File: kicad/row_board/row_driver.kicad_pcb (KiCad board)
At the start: 2 copper layers, 100 x 100 mm, 80 parts, among them J1 Panel row connector (female), J2 Row daisy chain connector (ma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, J3 Conn_01x04, J4 Column Board Connector, J6 Barrel_Jack, J7 Controller A, J8 Controller B, Q1 2N3904, Q2 FQP47P06, U1 TPIC6B595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

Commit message: Mostly routed column board
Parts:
- J2: footprint Connectors:IDC_Header_Straight_40pins -> lib_fp:IDC_Header_Straight_40pins
- J4: footprint Connectors:IDC_Header_Straight_10pins -> lib_fp:IDC_Header_Straight_10pins
- moved J4 2.95 mm to (30.0, 65.0)
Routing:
- net RC_DATA: track 66.6 -> 70.7 mm
- net RC_SHIFT_CLK: track 161.7 -> 165.8 mm
- net GND: track 37.1 -> 34.1 mm, vias 24 -> 23
- net COL_REG_CLK: track 53.5 -> 56.4 mm
- net ~RC_CLEAR: track 146.0 -> 144.5 mm, vias 8 -> 9

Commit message: Add Gerber and DXF files for row and column boards
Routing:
- net +5V: track 393.3 -> 404.1 mm
- net ~ROW_EN: track 112.4 -> 114.4 mm
- net Net-(D104-Pad2): track 50.8 -> 51.9 mm

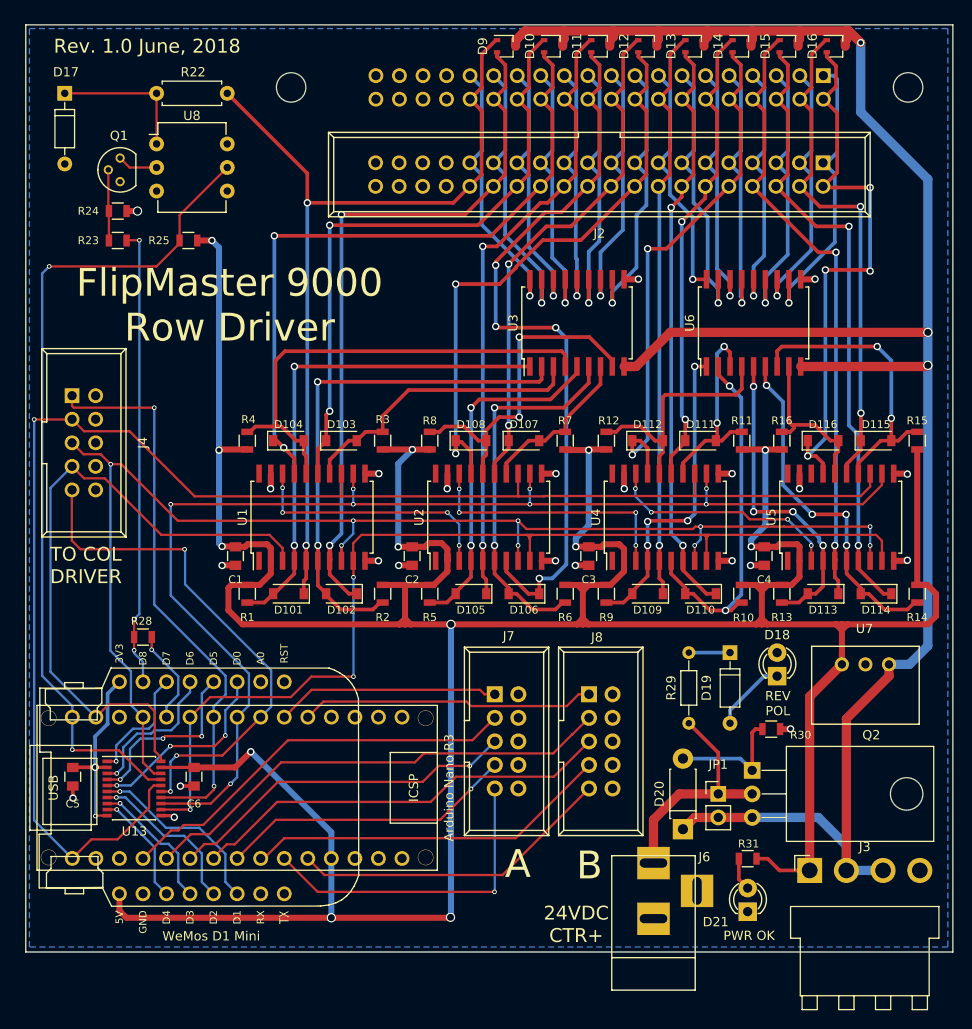
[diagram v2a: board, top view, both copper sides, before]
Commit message: Add project-local footprints and 3D models
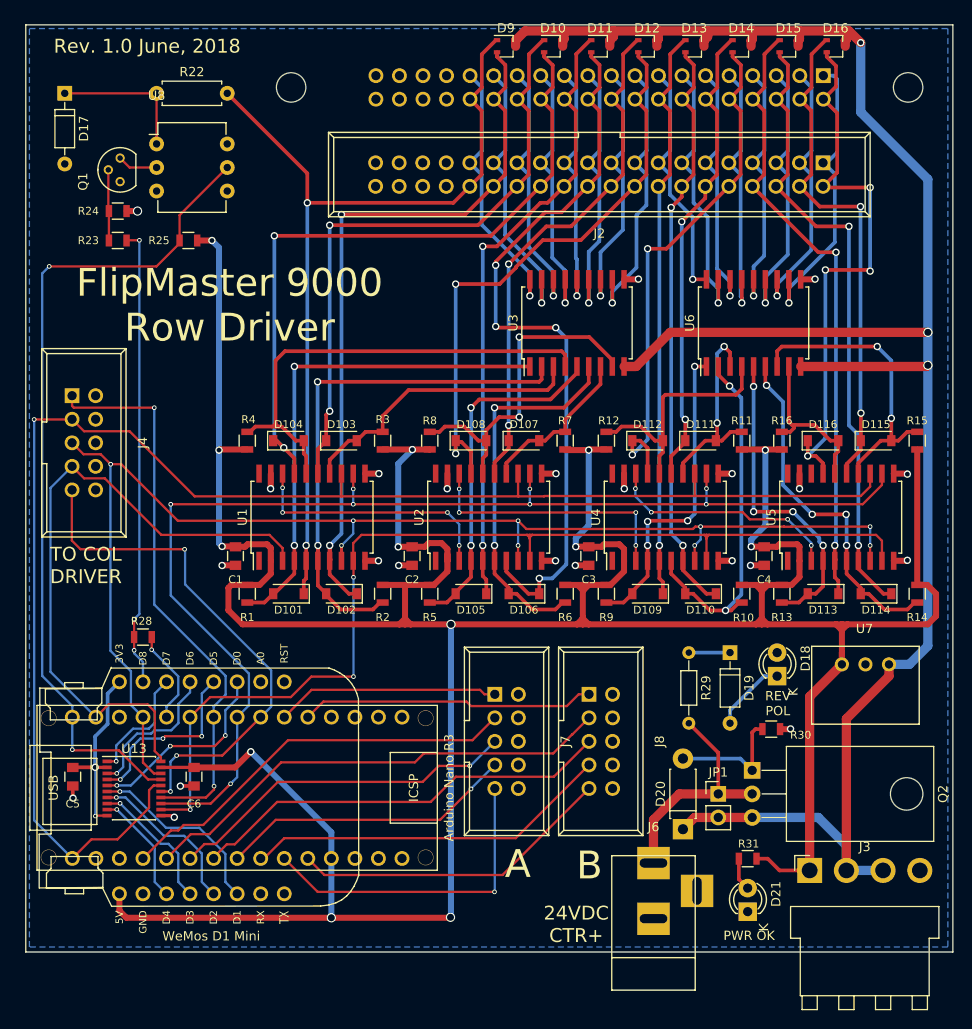
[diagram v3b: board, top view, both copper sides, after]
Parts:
- D10, D11, D12, D13, D14, D15, D16, D9: footprint TO_SOT_Packages_SMD:SOT-323_SC-70 -> lib_fp:SOT-323_SC-70
- D17, D19: footprint Diodes_THT:D_DO-35_SOD27_P7.62mm_Horizontal -> lib_fp:D_DO-35_SOD27_P7.62mm_Horizontal
- D18, D21: footprint LEDs:LED-3MM -> lib_fp:LED-3MM
- D20: footprint Diodes_THT:D_DO-41_SOD81_P7.62mm_Horizontal -> lib_fp:D_DO-41_SOD81_P7.62mm_Horizontal
- J3: footprint Connector_JST:JST_VH_B4PS-VH_1x04_P3.96mm_Horizontal -> lib_fp:JST_VH_B4PS-VH_1x04_P3.96mm_Horizontal
- J6: footprint Connectors:BARREL_JACK -> lib_fp:BARREL_JACK
- J7, J8: footprint Connectors:IDC_Header_Straight_10pins -> lib_fp:IDC_Header_Straight_10pins
- JP1: footprint Pin_Headers:Pin_Header_Straight_1x02_Pitch2.54mm -> lib_fp:Pin_Header_Straight_1x02_Pitch2.54mm
- Q1: footprint TO_SOT_Packages_THT:TO-92_Molded_Narrow -> lib_fp:TO-92_Molded_Narrow
- Q2: footprint TO_SOT_Packages_THT:TO-220_Horizontal -> lib_fp:TO-220_Horizontal
- R22: footprint Resistors_THT:R_Axial_DIN0207_L6.3mm_D2.5mm_P7.62mm_Horizontal -> lib_fp:R_Axial_DIN0207_L6.3mm_D2.5mm_P7.62mm_Horizontal
- R29: footprint Resistors_THT:R_Axial_DIN0204_L3.6mm_D1.6mm_P7.62mm_Horizontal -> lib_fp:R_Axial_DIN0204_L3.6mm_D1.6mm_P7.62mm_Horizontal
- U1, U2, U4, U5: footprint Housings_SOIC:SOIC-20W_7.5x12.8mm_Pitch1.27mm -> lib_fp:SOIC-20W_7.5x12.8mm_Pitch1.27mm
- U13: footprint Housings_SSOP:SSOP-20_4.4x6.5mm_Pitch0.65mm -> lib_fp:SSOP-20_4.4x6.5mm_Pitch0.65mm
- U3, U6: footprint Housings_SOIC:SOIC-18W_7.5x11.6mm_Pitch1.27mm -> lib_fp:SOIC-18W_7.5x11.6mm_Pitch1.27mm
- U8: footprint Housings_DIP:DIP-6_W7.62mm -> lib_fp:DIP-6_W7.62mm
